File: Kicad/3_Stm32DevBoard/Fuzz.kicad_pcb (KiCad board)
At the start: 2 copper layers, 100 x 82 mm, 114 parts, among them J1 Audio In/Out JST XH, J10 JST XH Buttons, J11 LCD JST XH, J12 Bypass Switch JST XH, J2 TONE_POTS, J3 Jumper BOOT0, J4 VOL POT A100K JST XH, J5 PowerTest_PinHeader, J6 9V Power JST XH, J7 UART Pin Header, J8 Jumper BOOT1, J9 SWD, Q1 PN2222A, Q10 2SC1815, Q11 PN2222A, Q12 S9013, Q13 MMBT3904, Q14 S9018, Q15 BC848B, Q16 2SC1623, Q17 MPSA18, Q18 MMBT5551L, Q19 2N5088, Q2 MMBT3904, Q20 MMBTA42, Q21 BC807, Q22 BC846, Q23 BC847B, Q24 BC847C, Q25 BC848B, Q26 S9013, Q27 S9018, Q28 C945, Q29 2SC1623, Q3 MMBT5551L, Q30 2SC1815, Q31 MPSA18, Q32 2N5088, Q4 MMBTA42, Q5 BC807, Q6 BC846, Q7 BC847B, Q8 BC847C, Q9 C945, SW1 RESET, U1 AMS1117-5.0, U2 AMS1117-3.3, U21 CD4051BM, U22 CD4504BM, U23 CD4504BM, U24 CD4054BM, U25 CD4053BM, U3 STM32F103C8Tx, U4 CD4051BM, U6 CD4067BM, U7 CD4067BM, U8 CD4067BM, U9 CD4067BM, Y1 8MHz

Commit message: STM32 Dev Board
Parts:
- removed C10, C7, C8, C9: 100nF, Capacitor_SMD:C_0805_2012Metric_Pad1.15x1.40mm_HandSolder
- removed C20: 10uF, Capacitor_SMD:C_0805_2012Metric_Pad1.15x1.40mm_HandSolder
- removed C5, C6: 20pF, Capacitor_SMD:C_0805_2012Metric_Pad1.15x1.40mm_HandSolder
- removed J3: Jumper BOOT0, Connector_PinHeader_2.54mm:PinHeader_1x03_P2.54mm_Vertical
- removed J8: Jumper BOOT1, Connector_PinHeader_2.54mm:PinHeader_1x03_P2.54mm_Vertical
- removed J9: SWD, Connector_PinHeader_2.54mm:PinHeader_1x06_P2.54mm_Vertical
- removed R7: 10K, Resistor_SMD:R_0805_2012Metric_Pad1.15x1.40mm_HandSolder
- removed the REF** at (45.7, 108.3)
- removed RN2: 33R, Resistor_SMD:R_Array_Convex_4x0603
- removed SW1: RESET, Button_Switch_SMD:SW_SPST_CK_RS282G05A3
- removed Y1: 8MHz, Crystal:Crystal_HC49-4H_Vertical
- added REF**: KiCad-Logo2_5mm_SilkScreen, Symbol:KiCad-Logo2_5mm_SilkScreen, F.Cu at (86.7, 73.4)
- R5: value 220R -> 33R; moved to F.Cu
- R6: value 10K -> 33R; moved to F.Cu
- U3: value STM32F103C8Tx -> ChinaBluePill; footprint Package_QFP:LQFP-48-1EP_7x7mm_P0.5mm_EP3.6x3.6mm_ThermalVias -> 3_Stm32DevBoard:BluePill_STM32F103C
- moved J7 46.5 mm to (40.6, 107.8), turned to 90 degrees
- moved R5 42.2 mm to (42.5, 40.5), turned to 0 degrees
- moved R6 34.3 mm to (47.2, 40.5), turned to 0 degrees
- moved U3 26.4 mm to (34.1, 53.2), turned to 0 degrees
- moved J5 26.1 mm to (58.5, 57.4), turned to 90 degrees
- moved U22 23.9 mm to (60.4, 81.3)
- moved C2 22.6 mm to (53.8, 41.0)
- moved C4 22.1 mm to (62.9, 50.3), turned to 0 degrees
- moved U25 22.1 mm to (60.4, 66.2)
- moved C3 21.8 mm to (63.0, 42.9), turned to 0 degrees
- moved C45 20.5 mm to (55.0, 68.1)
- moved C47 18.5 mm to (54.7, 82.8), turned to 90 degrees
- moved D1 16.7 mm to (42.5, 44.7), turned to 180 degrees
- moved U2 13.6 mm to (62.7, 50.4)
- moved FB1 13.4 mm to (48.8, 44.6), turned to 0 degrees
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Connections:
- J5 pad 1: +9V -> /+9V_SAFE
- R5 pad 1: /Mcu/OSC_OUT -> /Mcu/I2C1_SCL
- R5 pad 2: Net-(C6-Pad1) -> /Mcu/I2C1_SCL_MCU
- R6 pad 1: GND -> /Mcu/I2C1_SDA
- R6 pad 2: /Mcu/BOOT0 -> /Mcu/I2C1_SDA_MCU
- U3 pad 10: Net-(U3-Pad10) -> /TRANSISTOR_C_SELECTION_3_3V3
- U3 pad 11: /TRANSISTOR_C_SELECTION_1_3V3 -> Net-(U3-Pad11)
- U3 pad 12: /Mcu/BYPASS_SWITCH_3V3 -> /CAPACITOR_D_SELECTION_0_3V3
- U3 pad 13: /BYPASS_MODE_3V3 -> /TRANSISTOR_B_SELECTION_0_3V3
- U3 pad 14: /TRANSISTOR_C_SELECTION_2_3V3 -> /TRANSISTOR_B_SELECTION_1_3V3
- U3 pad 15: /TRANSISTOR_C_SELECTION_3_3V3 -> /CAPACITOR_A_SELECTION_0_3V3
- U3 pad 16: Net-(U3-Pad16) -> /CAPACITOR_A_SELECTION_1_3V3
- U3 pad 17: /CAPACITOR_D_SELECTION_0_3V3 -> Net-(U3-Pad17)
- U3 pad 18: /TRANSISTOR_B_SELECTION_0_3V3 -> Net-(U3-Pad18)
- U3 pad 19: /TRANSISTOR_B_SELECTION_1_3V3 -> GND
- U3 pad 20: /Mcu/BOOT1 -> GND
- U3 pad 21: /CAPACITOR_A_SELECTION_0_3V3 -> /CAPACITOR_A_SELECTION_2_3V3
- U3 pad 22: /CAPACITOR_A_SELECTION_1_3V3 -> Net-(U3-Pad22)
- U3 pad 23: +3V3 -> Net-(U3-Pad23)
- U3 pad 24: +3V3 -> Net-(U3-Pad24)
- U3 pad 25: /CAPACITOR_A_SELECTION_2_3V3 -> /TRANSISTOR_C_SELECTION_0_3V3
- U3 pad 26: Net-(U3-Pad26) -> /Mcu/UART_RX
- U3 pad 27: Net-(U3-Pad27) -> /Mcu/UART_TX
- U3 pad 28: Net-(U3-Pad28) -> /CAPACITOR_D_SELECTION_1_3V3
- U3 pad 29: /TRANSISTOR_C_SELECTION_0_3V3 -> /CAPACITOR_D_SELECTION_2_3V3
- U3 pad 30: /Mcu/UART_RX -> /Mcu/GPIO_BUTTON_DECREASE
- U3 pad 31: /Mcu/UART_TX -> Net-(U3-Pad31)
- U3 pad 32: /CAPACITOR_D_SELECTION_1_3V3 -> /Mcu/GPIO_BUTTON_INCREASE
- U3 pad 33: /CAPACITOR_D_SELECTION_2_3V3 -> /Mcu/GPIO_BUTTON_ENTER
- U3 pad 34: /Mcu/SYS_JTMS_SWDIO_MCU -> /Mcu/I2C1_SCL_MCU
- U3 pad 35: +3V3 -> /Mcu/I2C1_SDA_MCU
- U3 pad 36: +3V3 -> /TRANSISTOR_B_SELECTION_2_3V3
- U3 pad 37: /Mcu/SYS_JTICK_SWCLK_MCU -> /TRANSISTOR_B_SELECTION_3_3V3
- U3 pad 38: /Mcu/GPIO_BUTTON_DECREASE -> Net-(U3-Pad38)
- U3 pad 39: /Mcu/SYS_JTDO_TRACESWO -> GND
- U3 pad 40: /Mcu/GPIO_BUTTON_ENTER -> Net-(U3-Pad40)
- U3 pad 41: /Mcu/GPIO_BUTTON_INCREASE -> (no net)
- U3 pad 42: /Mcu/I2C1_SCL_MCU -> (no net)
- U3 pad 5: /Mcu/OSC_IN -> Net-(U3-Pad5)
- U3 pad 6: /Mcu/OSC_OUT -> /TRANSISTOR_C_SELECTION_1_3V3
- U3 pad 7: /Mcu/NRST -> /Mcu/BYPASS_SWITCH_3V3
- U3 pad 8: +3V3 -> /BYPASS_MODE_3V3
- U3 pad 9: Net-(U3-Pad9) -> /TRANSISTOR_C_SELECTION_2_3V3
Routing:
- net +3V3: track 262.3 -> 152.9 mm, vias 12 -> 2
- net /+9V_SAFE: track 367.4 -> 272.2 mm, vias 18 -> 15
- net /Mcu/BOOT1: track 52.3 -> 0.00 mm, vias 2 -> 0
- net /Mcu/NRST: track 43.1 -> 0.00 mm, vias 2 -> 0
- net /CAPACITOR_D_SELECTION_1_3V3: track 66.7 -> 27.7 mm, vias 6 -> 2
- net /AudioInOut/JACK_IN_SIGNAL: track 66.4 -> 104.9 mm
- net /TRANSISTOR_C_SELECTION_0_3V3: track 44.9 -> 10.1 mm, vias 5 -> 1
- net /CAPACITOR_A_SELECTION_2_3V3: track 23.8 -> 58.3 mm
- net /AudioInOut/JACK_OUT_SIGNAL: track 74.3 -> 107.7 mm
- net /Mcu/I2C1_SDA: track 40.0 -> 7.32 mm
- net /Mcu/I2C1_SCL: track 37.9 -> 6.72 mm
- net /Mcu/BOOT0: track 30.1 -> 0.00 mm, vias 3 -> 0
- net /CAPACITOR_D_SELECTION_2_3V3: track 59.5 -> 30.5 mm, vias 4 -> 0
- net /CAPACITOR_A_SELECTION_1: track 43.2 -> 71.7 mm, vias 2 -> 4
- net /CAPACITOR_A_SELECTION_2: track 44.2 -> 71.3 mm, vias 2 -> 4
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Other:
- board text added: "GUITAR PEDAL FUZZ 16K FUZZ V0.3"
- board text removed: "3V3 BT0 GND"
- board text removed: "3V3 BT1 GND"
- board text removed: "5V GND CLK"
- board text removed: "BOOT 0"
- board text removed: "BOOT 1"
- board text removed: "DIO SWO NRST"
- board text removed: "GUITAR PEDAL FUZZ EFFECT 16K FUZZ V0.2"
- board text removed: "LEVEL SHIFTER"
- board text removed: "OSCILLATOR CAPACITORS"
- board text removed: "PROGRAMMING, DEBUGGING AND TESTING"
- board text removed: "SWDIO"
- board text removed: "VOLTAGE"

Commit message: git ignore
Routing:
- net GND: vias 67 -> 68
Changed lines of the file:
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@@
     (thickness 1.6)
     (drawings 85)
-    (tracks 3130)
+    (tracks 3131)
     (zones 0)
     (modules 100)
@@
   (via (at 44.44 37.74) (size 0.6) (drill 0.4) (layers F.Cu B.Cu) (net 2))
   (via (at 47.35 38.58) (size 0.6) (drill 0.4) (layers F.Cu B.Cu) (net 2))
+  (via (at 33.6 46.56) (size 0.6) (drill 0.4) (layers F.Cu B.Cu) (net 2))
   (segment (start 59.45 42.78) (end 57.36 42.78) (width 0.381) (layer F.Cu) (net 3))
   (segment (start 56.799999 43.490001) (end 56.5 43.79) (width 0.381) (layer F.Cu) (net 3))

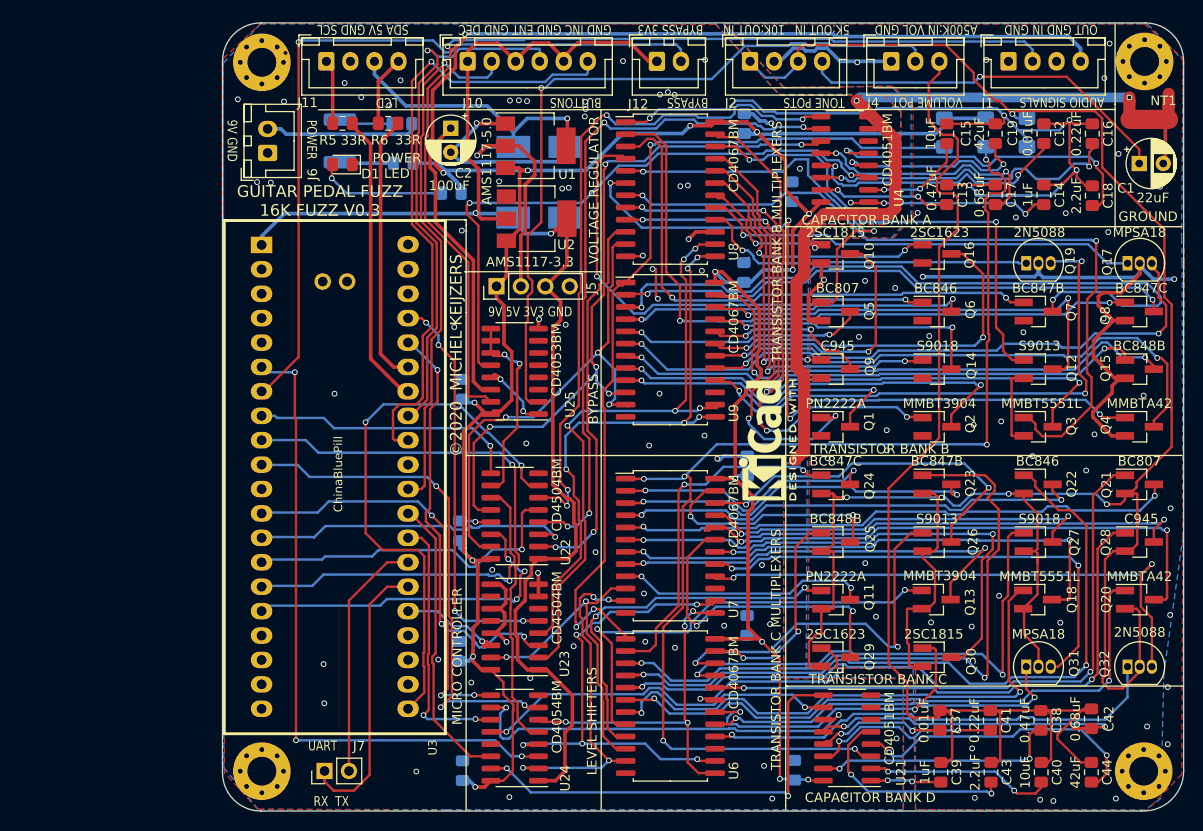
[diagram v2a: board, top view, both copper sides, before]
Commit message: Remove 3V3 voltage regulation (get from STM32 5V)
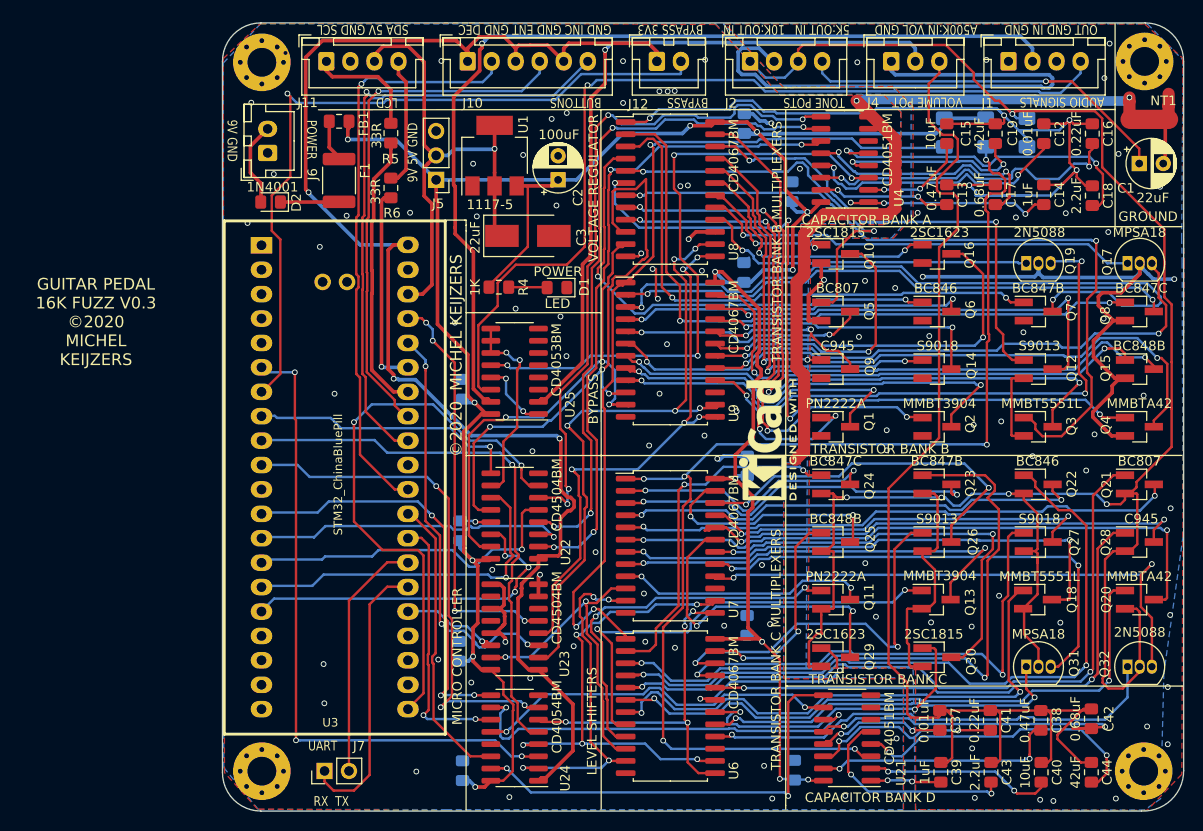
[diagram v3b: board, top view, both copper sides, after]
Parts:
- removed C4: 22uF, Diode_SMD:D_SMB_Handsoldering
- removed U2: AMS1117-3.3, Package_TO_SOT_SMD:SOT-223-3_TabPin2
- C3, D2, FB1, R4: moved to F.Cu
- F1: value Polyfuse 1.1A (1812L) -> Polyfuse; moved to F.Cu
- J5: footprint Connector_PinHeader_2.54mm:PinHeader_1x04_P2.54mm_Vertical -> Connector_PinHeader_2.54mm:PinHeader_1x03_P2.54mm_Vertical
- U1: value AMS1117-5.0 -> 1117-5
- U3: value ChinaBluePill -> STM32_ChinaBluePill
- moved D1 25.7 mm to (64.8, 57.5)
- moved D2 15.9 mm to (35.0, 48.6), turned to 180 degrees
- moved J5 12.7 mm to (52.2, 46.3), turned to 180 degrees
- moved C2 12.4 mm to (64.9, 46.3), turned to 90 degrees
- moved R4 11.0 mm to (58.8, 57.5), turned to 0 degrees
- moved C3 9.34 mm to (61.8, 52.2)
- moved FB1 7.97 mm to (42.1, 40.2)
- moved R6 6.73 mm to (47.5, 47.2), turned to 270 degrees
- moved R5 5.13 mm to (47.5, 41.5), turned to 270 degrees
- moved U1 4.41 mm to (58.3, 43.8), turned to 90 degrees
- moved F1 4.12 mm to (42.1, 46.4), turned to 90 degrees
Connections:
- J5 pad 3: +3V3 -> GND
- U3 pad 1: +3V3 -> Net-(U3-Pad1)
- U3 pad 38: Net-(U3-Pad38) -> +5V
- U3 pad 40: Net-(U3-Pad40) -> +3V3
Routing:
- net GNDA: track 98.2 -> 143.4 mm
- net GND: track 133.2 -> 111.0 mm, vias 68 -> 66
- net /TRANSISTOR_B_SELECTION_0: track 46.5 -> 61.4 mm
- net /AudioInOut/JACK_OUT_SIGNAL: track 107.7 -> 94.8 mm
- net /+9V_SAFE: track 272.2 -> 283.0 mm, vias 15 -> 14
- net Net-(D1-Pad2): track 13.5 -> 4.02 mm, vias 1 -> 0
- net +9V: track 16.1 -> 8.82 mm
- net /Mcu/I2C1_SDA_MCU: track 28.2 -> 21.2 mm, vias 0 -> 1
- net /Mcu/I2C1_SDA: track 7.32 -> 13.5 mm
- net /Mcu/I2C1_SCL: track 6.72 -> 12.9 mm
- net /Mcu/GPIO_BUTTON_DECREASE: track 55.4 -> 61.2 mm
- net /AudioInOut/JACK_IN_SIGNAL: track 104.9 -> 99.8 mm
- net /JACK_OUT_SIGNAL_FROM_FUZZ: track 77.4 -> 74.0 mm
- net /Mcu/BYPASS_SWITCH_3V3: track 80.4 -> 77.1 mm
- net /TRANSISTOR_B_SELECTION_3: track 60.2 -> 57.8 mm
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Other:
- board text added: "9V 5V GND"
- board text added: "GUITAR PEDAL 16K FUZZ V0.3 ©2020 MICHEL KEIJZERS"
- board text added: "LED"
- board text removed: "9V 5V 3V3 GND"
- board text removed: "GUITAR PEDAL FUZZ 16K FUZZ V0.3"
- board text removed: "POWER LED"
